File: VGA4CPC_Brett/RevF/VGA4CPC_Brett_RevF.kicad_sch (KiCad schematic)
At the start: 51 parts, among them J1 CPC VIDEO IN, J2 LUM OUT, J3 +5V IN, J4 VFREQ, J5 SPARE GPIO, J6 VGA OUT, J7 CPC PLUS VIDEO IN, J8 CPC PLUS AUDIO OUT, SW1 RESET, SW2 WACKED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

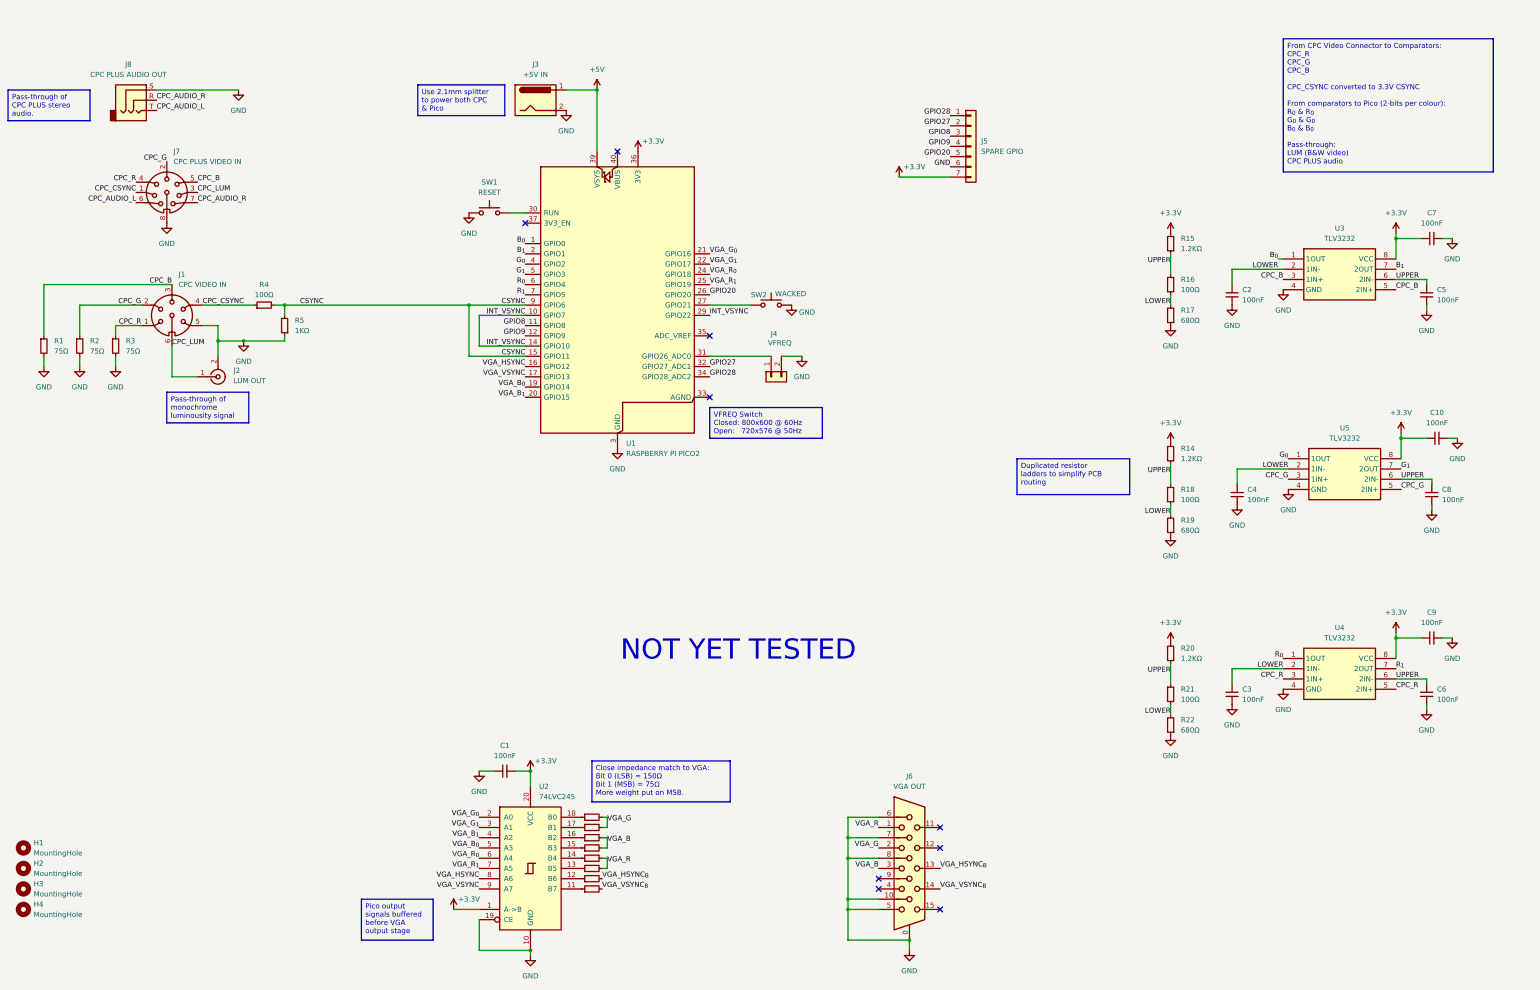
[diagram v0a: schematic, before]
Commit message: Rev. F initial commit
Moved comparator to own daughterboard
Switched from 3.3V to 5V logic (requires Pico 2 for sure)
Switched 74LVC245 (SMD) to 74HCT245 (through-hole)
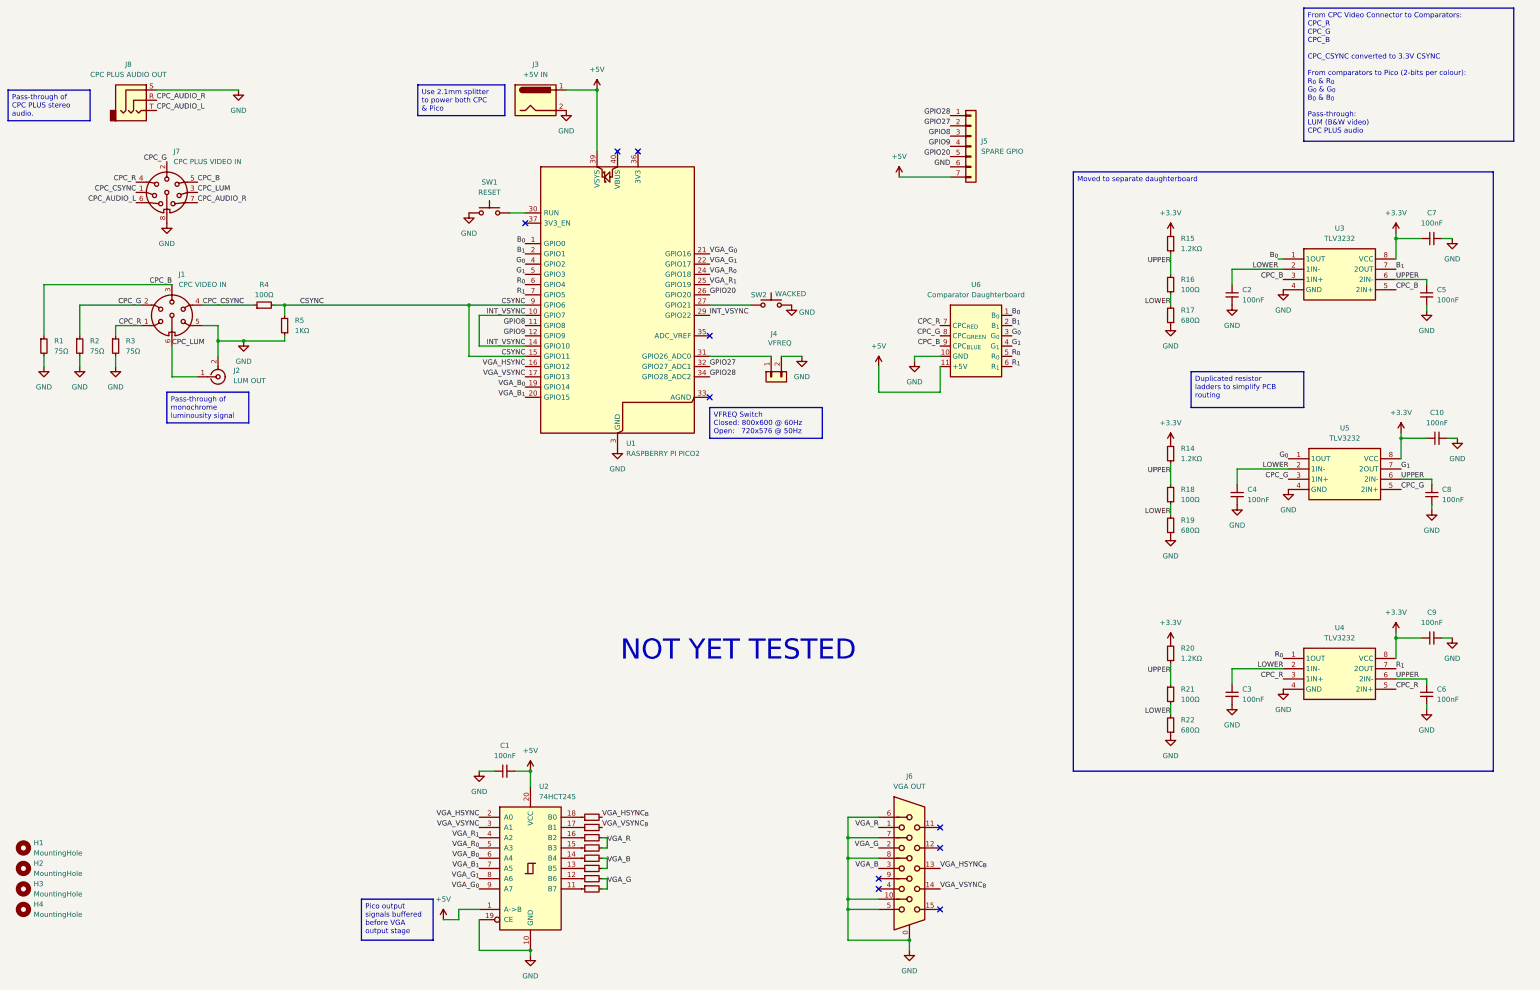
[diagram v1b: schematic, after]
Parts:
- added U6: Comparator Daughterboard, VGA4CPC_Footprints:Comparator Daughterboard, symbol VGA4CPC_Symbols:Comparator_Daughterboard
- R10, R6, R9: value 150Ω -> 820Ω
- R11, R7, R8: value 75Ω -> 820Ω
- U2: value 74LVC245 -> 74HCT245; footprint Package_SO:SOIC-20W_7.5x12.8mm_P1.27mm -> Package_DIP:DIP-20_W7.62mm
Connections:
- net +3.3V: no longer C1.2, J5.7 (Pin_7), U1.36 (3V3), U2.1 (A->B), U2.20 (VCC)
- net +5V: now also C1.2, J5.7 (Pin_7), U2.1 (A->B), U2.20 (VCC), U6.11 (+5V)
- net B_{0}: now also U6.1 (B_{0})
- net B_{1}: now also U6.2 (B_{1})
- net CPC_B: now also U6.9 (CPC_{BLUE})
- net CPC_G: now also U6.8 (CPC_{GREEN})
- net CPC_R: now also U6.7 (CPC_{RED})
- net GND: now also U6.10 (GND)
- net G_{0}: now also U6.3 (G_{0})
- net G_{1}: now also U6.4 (G_{1})
- net R_{0}: now also U6.5 (R_{0})
- net R_{1}: now also U6.6 (R_{1})
- net VGA_B_{0}: now also U2.6 (A4); no longer U2.5 (A3)
- net VGA_B_{1}: now also U2.7 (A5); no longer U2.4 (A2)
- net VGA_G_{0}: now also U2.9 (A7); no longer U2.2 (A0)
- net VGA_G_{1}: now also U2.8 (A6); no longer U2.3 (A1)
- net VGA_HSYNC: now also U2.2 (A0); no longer U2.8 (A6)
- net VGA_R_{0}: now also U2.5 (A3); no longer U2.6 (A4)
- net VGA_R_{1}: now also U2.4 (A2); no longer U2.7 (A5)
- net VGA_VSYNC: now also U2.3 (A1); no longer U2.9 (A7)
- net at R7.1: now also U2.11 (B7); no longer U2.17 (B1)
- net at R13.1: now also U2.17 (B1); no longer U2.11 (B7)
- net at R9.1: now also U2.13 (B5); no longer U2.15 (B3)
- net at R8.1: now also U2.14 (B4); no longer U2.16 (B2)
- net at R10.1: now also U2.16 (B2); no longer U2.14 (B4)
- net at R11.1: now also U2.15 (B3); no longer U2.13 (B5)
- net at R6.1: now also U2.12 (B6); no longer U2.18 (B0)
- net at R12.1: now also U2.18 (B0); no longer U2.12 (B6)
- no-connect marks 9 -> 10
